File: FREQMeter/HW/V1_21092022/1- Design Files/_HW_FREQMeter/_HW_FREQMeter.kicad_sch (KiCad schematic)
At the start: 0 parts

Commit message: WORKING ON FREQMeter Hardware
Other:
- added sheet 7SEGMENT_LEDs_PWR ([05] - 7SEGMENT_LEDs_PWRDIST.kicad_sch)
- added sheet BIN CNTR LEDs ([06] - LEDs.kicad_sch)
- added sheet MCU - PB ([03] - MCU_PB.kicad_sch)
- added sheet SIG INPUT ([04] - SIG INPUT.kicad_sch)

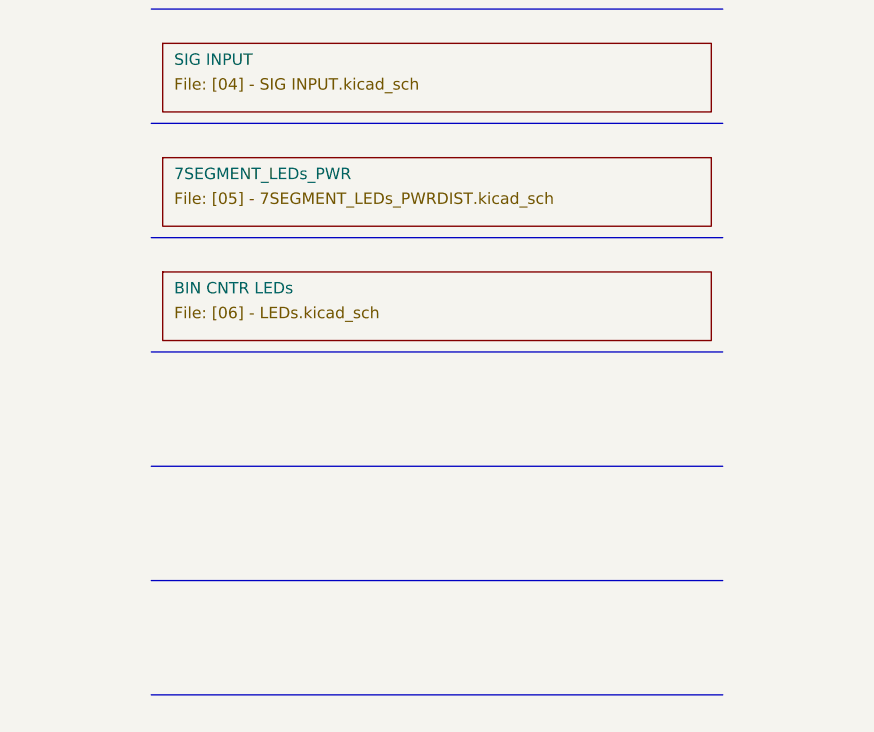
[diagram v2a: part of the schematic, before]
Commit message: frequency meter input schematic in progress
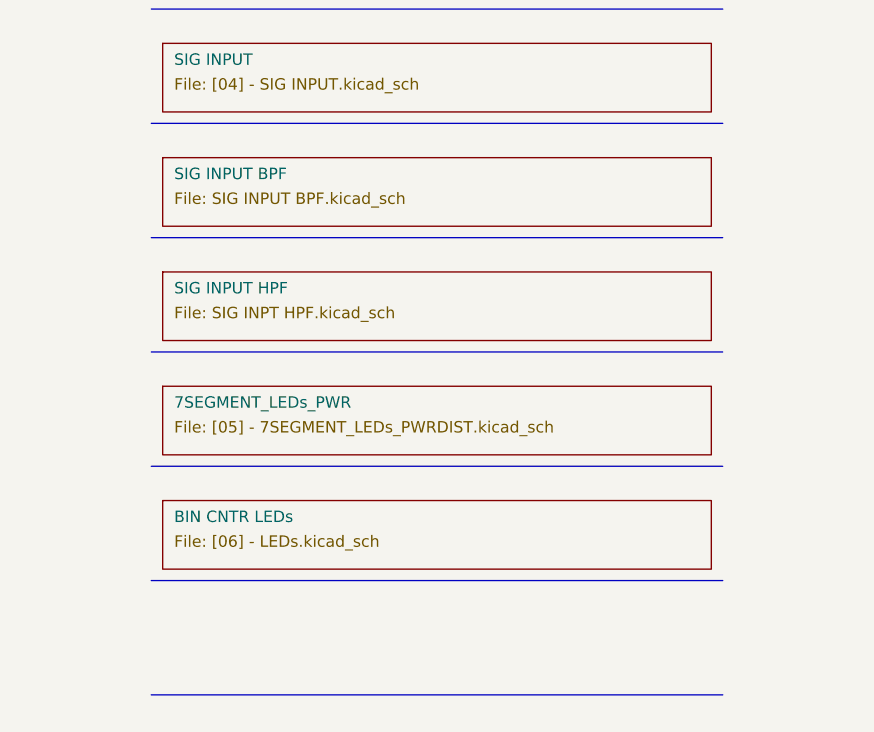
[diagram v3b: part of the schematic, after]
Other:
- added sheet SIG INPUT BPF (SIG INPUT BPF.kicad_sch)
- added sheet SIG INPUT HPF (SIG INPT HPF.kicad_sch)
